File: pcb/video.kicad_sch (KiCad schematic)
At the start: 15 parts, among them J5 VGA, Q4 2N7000, Q5 2N7000, Q6 2N7000, U10 74HC00, U11 4053, U12 74HC157, U13 74HC139, U14 74HC157, U15 74AC573, X1 25.175MHz

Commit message: WIP schematic
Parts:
- removed J5: VGA, symbol Connector:DE15_Receptacle_HighDensity_MountingHoles
- added J5: VGA, symbol Connector:DE15_Socket_HighDensity_MountingHoles
- X1: footprint Oscillator:Oscillator_DIP-8_LargePads -> Oscillator:Oscillator_DIP-8
- renumbered U10 to U11, U11 to U12, U12 to U13, U13 to U2
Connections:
- net GND: now also J5.0, J5.10, J5.5, J5.6, J5.7, J5.8
- net R2R Blue/OUT: now also J5.3
- net R2R Green/OUT: now also J5.2
- net R2R Red/OUT: now also J5.1
- net ~{HSYNC}: now also J5.13
- net ~{VSYNC}: now also J5.14
- no-connect marks 9 -> 13

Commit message: WIP schematic
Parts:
- added C12, C13: 100nF, symbol Device:C_Small
- added J6: SHIELD, symbol Connector:Conn_01x01_Pin
- added unit 5 of U11
- added U15: 74HC04, symbol 74xx:74HC04
- renumbered U15 to U16
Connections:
- net +5V: now also C12.2, C13.2, U11.14 (VCC), U15.14 (VCC)
- net GND: now also C12.1, C13.1, U11.7 (GND), U15.7 (GND); no longer J5.0
- new net: J5.0, J6.1 (Pin_1)
- no-connect marks 13 -> 14

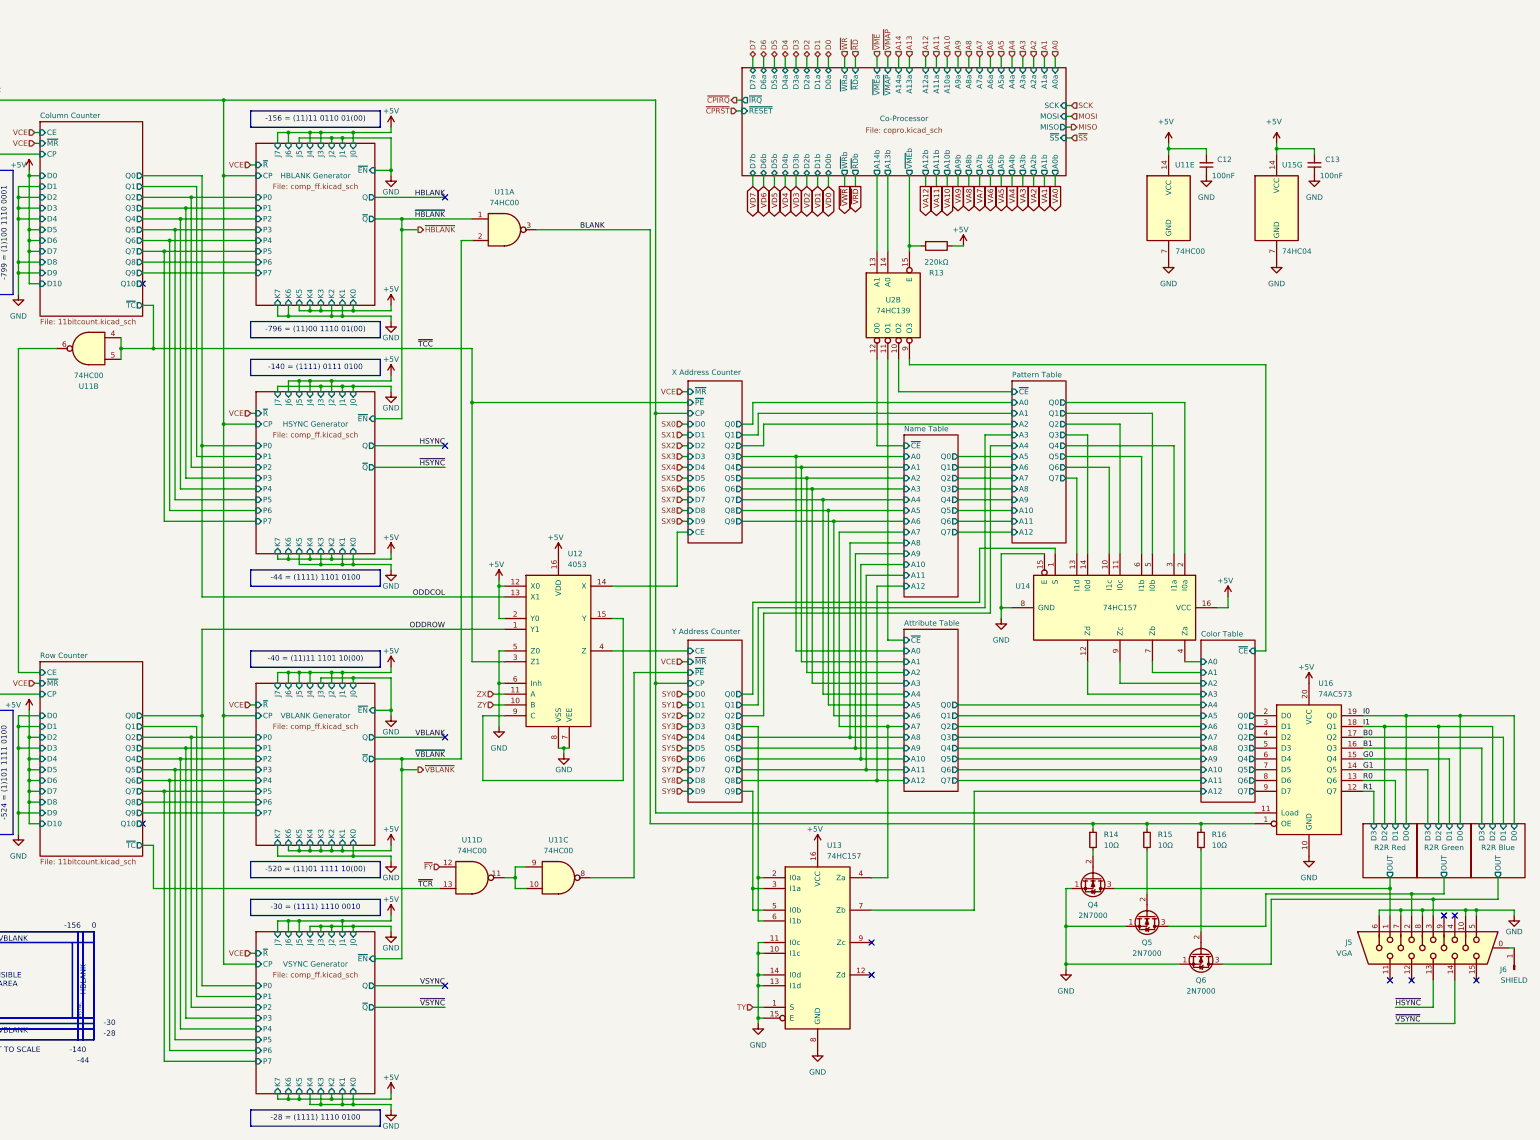
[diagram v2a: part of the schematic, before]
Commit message: WIP PCB (add bypass caps, minor fixes)
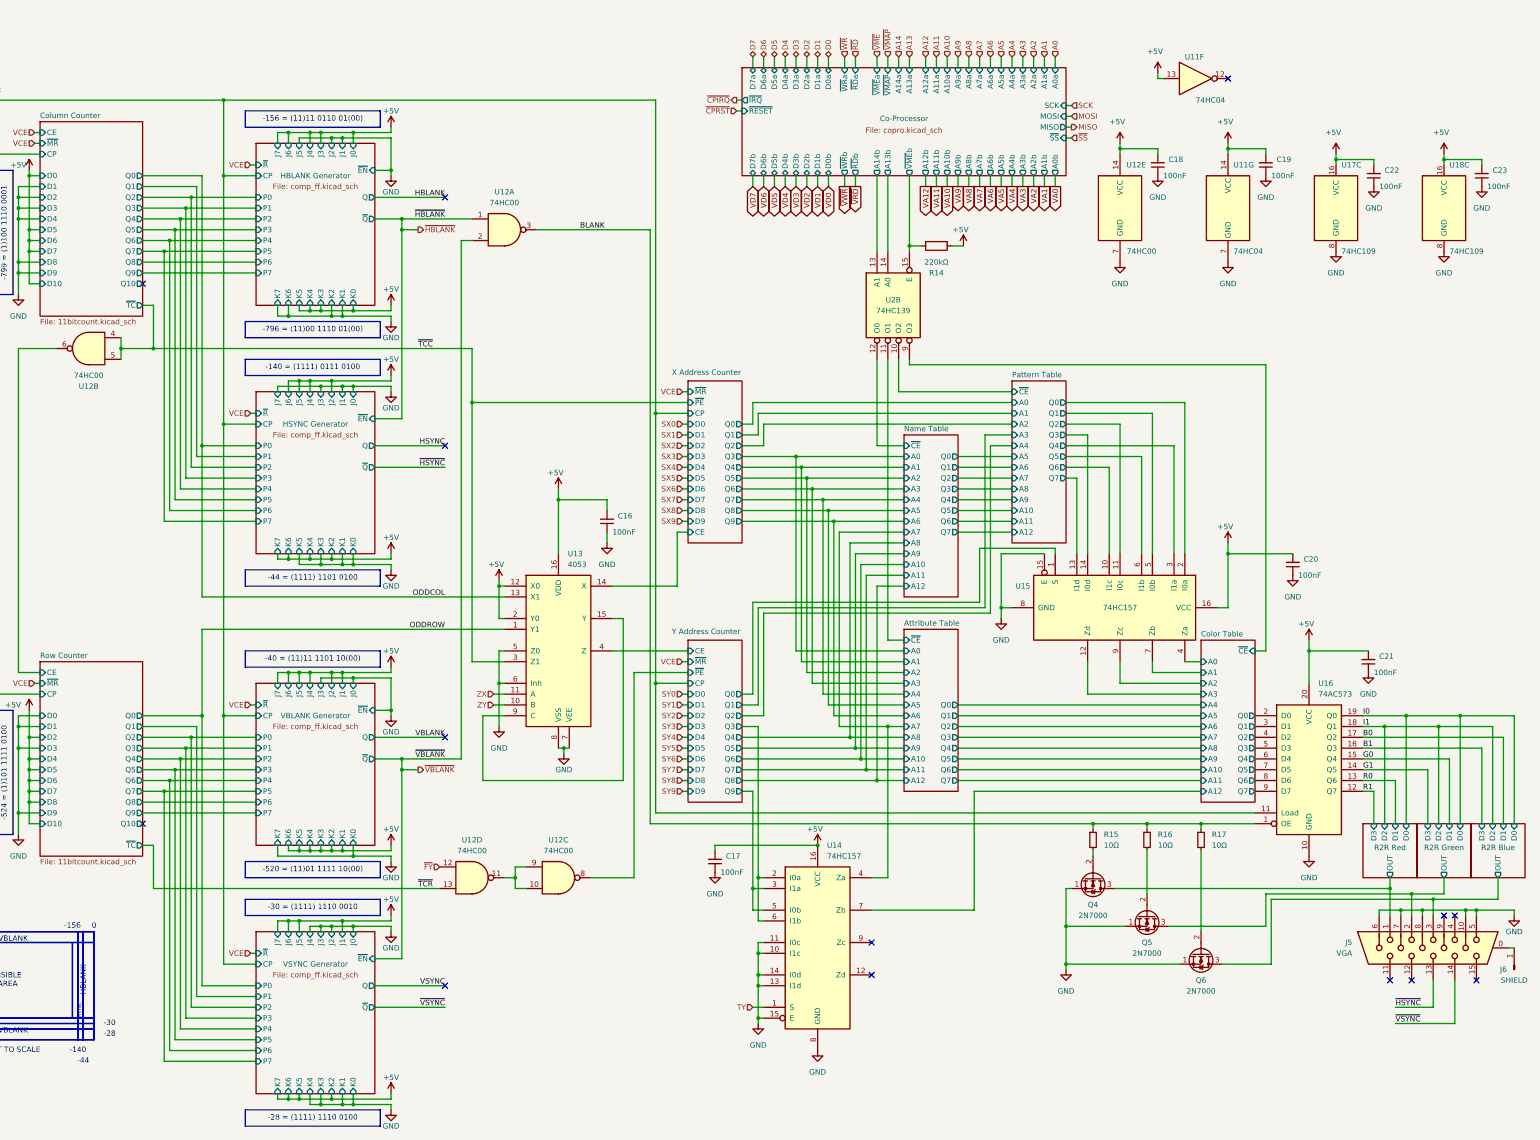
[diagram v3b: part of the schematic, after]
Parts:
- added C16, C17, C20, C21, C22, C23: 100nF, symbol Device:C_Small
- added unit 6 of U11
- added U17, U18: 74HC109, symbol 74xx:74LS109
- renumbered C12 to C18, C13 to C19, R13 to R14, R14 to R15, R15 to R16, R16 to R17, U15 to U11, U11 to U12, U12 to U13, U13 to U14, U14 to U15
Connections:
- net +5V: now also C16.2, C17.2, C20.2, C21.2, C22.2, C23.2, U11.13, U17.16 (VCC), U18.16 (VCC)
- net GND: now also C16.1, C17.1, C20.1, C21.1, C22.1, C23.1, U17.8 (GND), U18.8 (GND)
- no-connect marks 14 -> 15
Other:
- moved on the sheet: C18, C19, U11G, U12E
